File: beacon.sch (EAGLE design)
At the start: 23 parts, among them IC1 MEGA48/88/168-AU, X1 MINI-USB-SCHIELD-32005-301

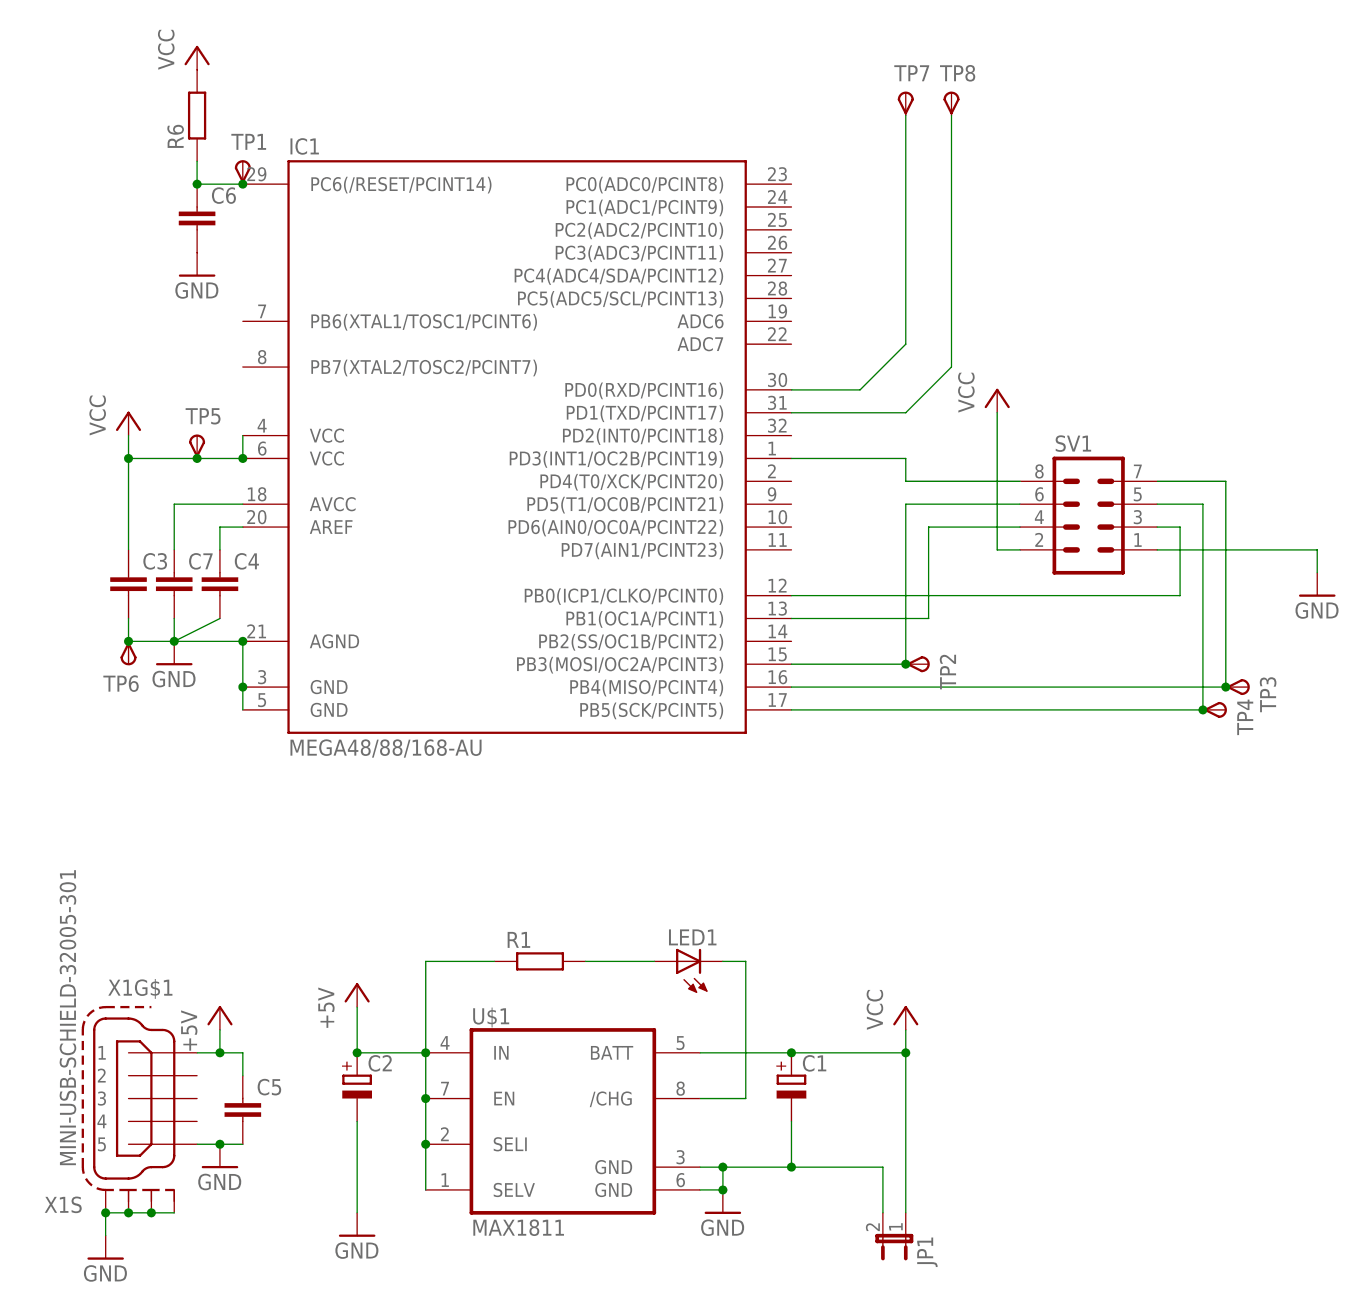
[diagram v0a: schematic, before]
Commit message: update name+value
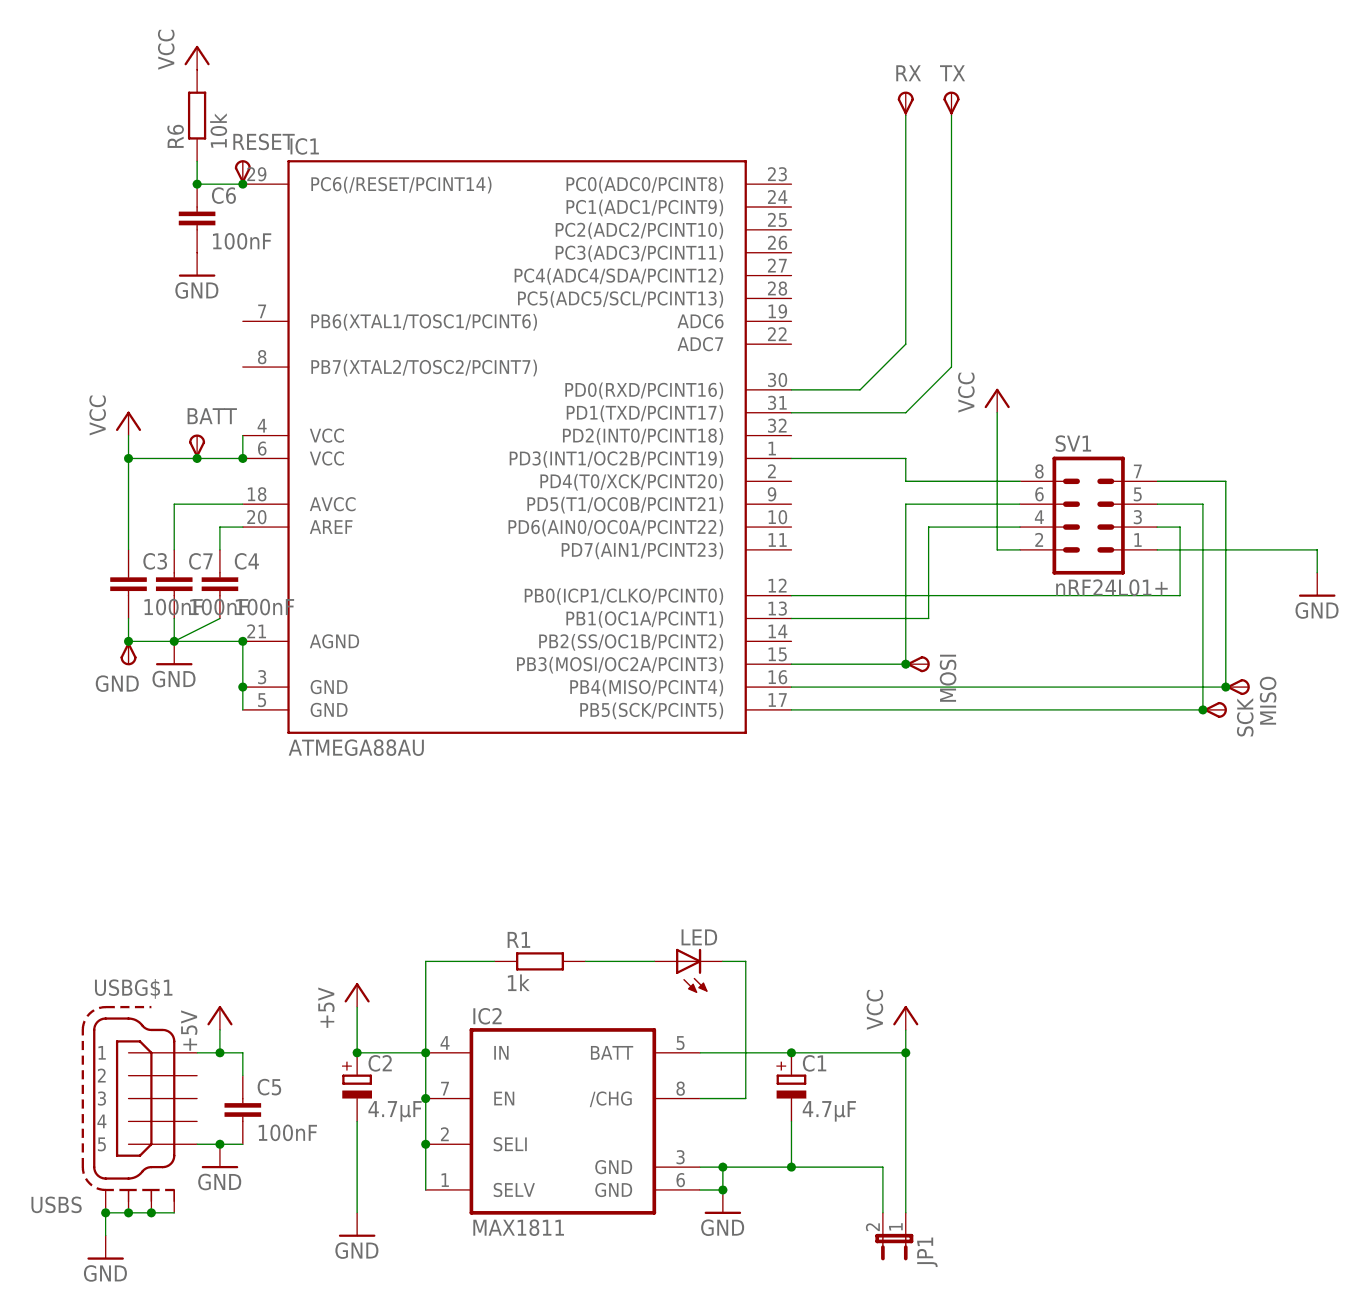
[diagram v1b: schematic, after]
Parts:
- C1, C2: value (none) -> 4.7μF
- C3, C4, C5, C6, C7: value (none) -> 100nF
- IC1: value MEGA48/88/168-AU -> ATMEGA88AU
- R1: value (none) -> 1k
- R6: value (none) -> 10k
- SV1: value (none) -> nRF24L01+
- renumbered LED1 to LED, TP1 to RESET, TP2 to MOSI, TP3 to MISO, TP4 to SCK, TP5 to BATT, TP6 to GND, TP7 to RX, TP8 to TX, U$1 to IC2, X1 to USB
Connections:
- net N$1 renamed AVCC
- net N$10 renamed PB1
- net N$11 renamed RESET
- net N$13 renamed PB0
- net N$14 renamed SCK
- net N$15 renamed MISO
- net N$2 renamed RX
- net N$5 renamed TX
- net N$6 renamed INT1
- net N$7 renamed AREF
- net N$9 renamed MOSI
